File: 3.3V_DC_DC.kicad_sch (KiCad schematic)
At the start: 10 parts, among them U5 MT2492

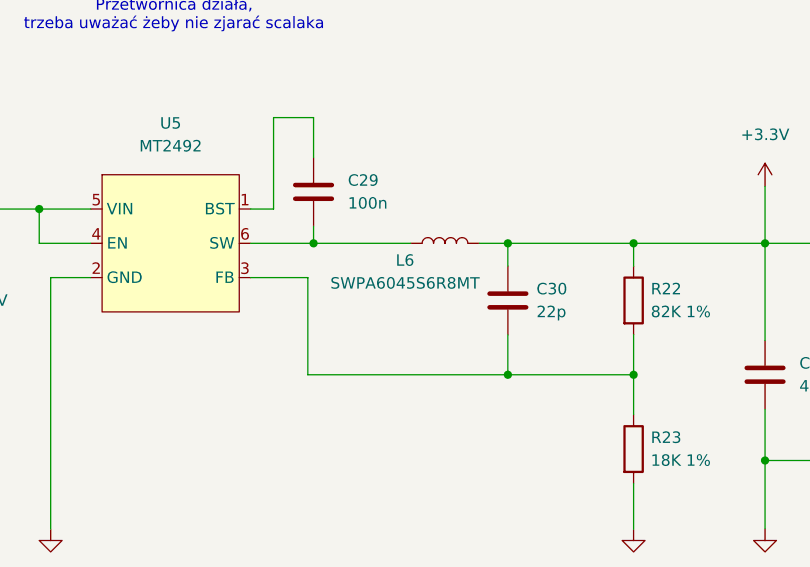
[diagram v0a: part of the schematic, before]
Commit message: Update schematic for V1.1
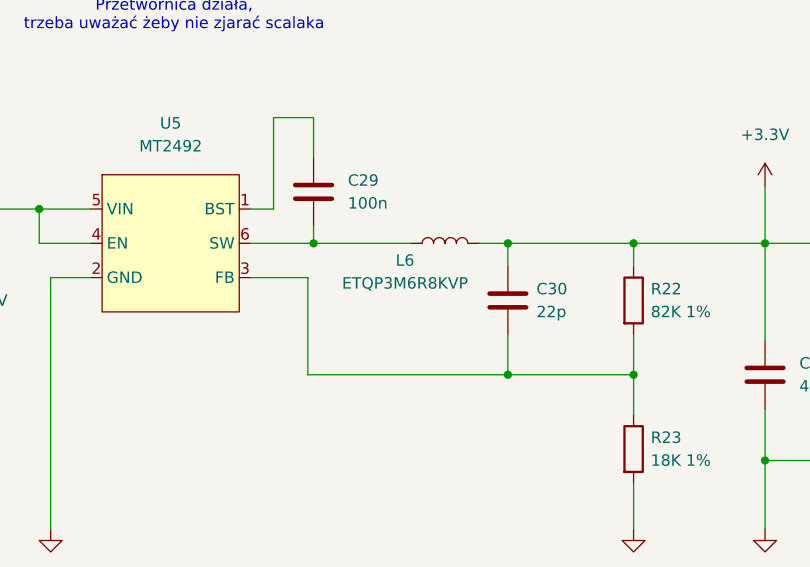
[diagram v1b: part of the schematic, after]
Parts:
- L6: value SWPA6045S6R8MT -> ETQP3M6R8KVP; footprint SWPA6045S6R8MT:SWPA6045S6R8MT -> panasonic_coil:IND_PCC-M0530M-LP_PAN; LCSC C57254 -> C412311
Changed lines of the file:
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@@
 			)
 		)
-		(property "Value" "SWPA6045S6R8MT"
+		(property "Value" "ETQP3M6R8KVP"
 			(at 132.08 58.42 90)
 			(effects
@@
 			)
 		)
-		(property "Footprint" "SWPA6045S6R8MT:SWPA6045S6R8MT"
+		(property "Footprint" "panasonic_coil:IND_PCC-M0530M-LP_PAN"
 			(at 136.525 53.975 0)
 			(effects
@@
 			)
 		)
-		(property "Datasheet" ""
+		(property "Datasheet" "https://www.lcsc.com/datasheet/lcsc_datasheet_1912111437_PANASONIC-ETQP3M6R8KVP_C412311.pdf"
 			(at 136.525 53.975 0)
 			(effects
@@
 			)
 		)
-		(property "LCSC" "C57254"
+		(property "LCSC" "C412311"
 			(at 136.525 53.975 90)
 			(effects

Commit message: DO the bulk of rev 1.2 layout
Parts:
- D7: value 3.3 -> PESD3V3L1BA; footprint Diode_SMD:D_SMA-SMB_Universal_Handsoldering -> Diode_SMD:D_SOD-323
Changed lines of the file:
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@@
 			)
 		)
-		(property "Value" "3.3"
+		(property "Value" "PESD3V3L1BA"
 			(at 193.675 67.9449 90)
 			(effects
@@
 			)
 		)
-		(property "Footprint" "Diode_SMD:D_SMA-SMB_Universal_Handsoldering"
+		(property "Footprint" "Diode_SMD:D_SOD-323"
 			(at 191.135 66.675 0)
 			(effects

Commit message: Use kicad symbol for the optotransistor
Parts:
- L6: footprint panasonic_coil:IND_PCC-M0530M-LP_PAN -> project_footprints:IND_PCC-M0530M-LP_PAN
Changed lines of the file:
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@@
 			)
 		)
-		(property "Footprint" "panasonic_coil:IND_PCC-M0530M-LP_PAN"
+		(property "Footprint" "project_footprints:IND_PCC-M0530M-LP_PAN"
 			(at 136.525 53.975 0)
 			(effects

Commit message: BOM updates
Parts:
- D7: LCSC (none) -> C2687129

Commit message: Zamkonator rev 1.3
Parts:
- renumbered C27 to C29, C28 to C30, C29 to C31, C30 to C32, C31 to C33, D7 to D12, R22 to R29, R23 to R30, U5 to U6
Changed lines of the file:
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@@
 		(dnp no)
 		(fields_autoplaced yes)
-		(property "Reference" "#PWR042"
+		(property "Reference" "#PWR080"
 			(at 172.085 92.075 0)
 			(hide yes)
@@
 			(project "Zamkonator"
 				(path "/727d6c0a-a0ef-4feb-9656-3db3cb90564a/8f37bbe0-86b5-4d99-ba58-4681edf3128e"
-					(reference "#PWR042")
+					(reference "#PWR080")
 					(unit 1)
 				)
@@
 		(dnp no)
 		(fields_autoplaced yes)
-		(property "Reference" "#PWR041"
+		(property "Reference" "#PWR079"
 			(at 172.085 51.435 0)
 			(hide yes)
@@
 			(project "Zamkonator"
 				(path "/727d6c0a-a0ef-4feb-9656-3db3cb90564a/8f37bbe0-86b5-4d99-ba58-4681edf3128e"
-					(reference "#PWR041")
+					(reference "#PWR079")
 					(unit 1)
 				)
@@
 		(dnp no)
 		(fields_autoplaced yes)
-		(property "Reference" "#PWR037"
+		(property "Reference" "#PWR075"
 			(at 59.055 92.075 0)
 			(hide yes)
@@
 			(project "Zamkonator"
 				(path "/727d6c0a-a0ef-4feb-9656-3db3cb90564a/8f37bbe0-86b5-4d99-ba58-4681edf3128e"
-					(reference "#PWR037")
+					(reference "#PWR075")
 					(unit 1)
 				)
@@
 		(dnp no)
 		(fields_autoplaced yes)
-		(property "Reference" "D7"
+		(property "Reference" "D12"
 			(at 193.675 65.4049 90)
 			(show_name no)
@@
 			(project "Zamkonator"
 				(path "/727d6c0a-a0ef-4feb-9656-3db3cb90564a/8f37bbe0-86b5-4d99-ba58-4681edf3128e"
-					(reference "D7")
+					(reference "D12")
 					(unit 1)
 				)
@@
 		(dnp no)
 		(fields_autoplaced yes)
-		(property "Reference" "C31"
+		(property "Reference" "C33"
 			(at 175.895 67.3099 0)
 			(show_name no)
@@
 			(project "Zamkonator"
 				(path "/727d6c0a-a0ef-4feb-9656-3db3cb90564a/8f37bbe0-86b5-4d99-ba58-4681edf3128e"
-					(reference "C31")
+					(reference "C33")
 					(unit 1)
 				)
@@
 		(dnp no)
 		(fields_autoplaced yes)
-		(property "Reference" "U5"
+		(property "Reference" "U6"
 			(at 106.045 40.64 0)
 			(show_name no)
@@
 			(project "Zamkonator"
 				(path "/727d6c0a-a0ef-4feb-9656-3db3cb90564a/8f37bbe0-86b5-4d99-ba58-4681edf3128e"
-					(reference "U5")
+					(reference "U6")
 					(unit 1)
 				)
@@
 		(dnp no)
 		(fields_autoplaced yes)
-		(property "Reference" "C29"
+		(property "Reference" "C31"
 			(at 125.73 46.9899 0)
 			(show_name no)
@@
 			(project "Zamkonator"
 				(path "/727d6c0a-a0ef-4feb-9656-3db3cb90564a/8f37bbe0-86b5-4d99-ba58-4681edf3128e"
-					(reference "C29")
+					(reference "C31")
 					(unit 1)
 				)
@@
 		(dnp no)
 		(fields_autoplaced yes)
-		(property "Reference" "R22"
+		(property "Reference" "R29"
 			(at 159.385 59.0549 0)
 			(show_name no)
@@
 			(project "Zamkonator"
 				(path "/727d6c0a-a0ef-4feb-9656-3db3cb90564a/8f37bbe0-86b5-4d99-ba58-4681edf3128e"
-					(reference "R22")
+					(reference "R29")
 					(unit 1)
 				)
@@
 		(dnp no)
 		(fields_autoplaced yes)
-		(property "Reference" "#PWR039"
+		(property "Reference" "#PWR077"
 			(at 92.71 92.075 0)
 			(hide yes)
@@
 			(project "Zamkonator"
 				(path "/727d6c0a-a0ef-4feb-9656-3db3cb90564a/8f37bbe0-86b5-4d99-ba58-4681edf3128e"
-					(reference "#PWR039")
+					(reference "#PWR077")
 					(unit 1)
 				)
@@
 		(dnp no)
 		(fields_autoplaced yes)
-		(property "Reference" "#PWR038"
+		(property "Reference" "#PWR076"
 			(at 76.835 92.075 0)
 			(hide yes)
@@
 			(project "Zamkonator"
 				(path "/727d6c0a-a0ef-4feb-9656-3db3cb90564a/8f37bbe0-86b5-4d99-ba58-4681edf3128e"
-					(reference "#PWR038")
+					(reference "#PWR076")
 					(unit 1)
 				)
@@
 		(dnp no)
 		(fields_autoplaced yes)
-		(property "Reference" "#PWR040"
+		(property "Reference" "#PWR078"
 			(at 157.48 92.075 0)
 			(hide yes)
@@
 			(project "Zamkonator"
 				(path "/727d6c0a-a0ef-4feb-9656-3db3cb90564a/8f37bbe0-86b5-4d99-ba58-4681edf3128e"
-					(reference "#PWR040")
+					(reference "#PWR078")
 					(unit 1)
 				)
@@
 		(dnp no)
 		(fields_autoplaced yes)
-		(property "Reference" "C27"
+		(property "Reference" "C29"
 			(at 62.865 57.5309 0)
 			(show_name no)
@@
 			(project "Zamkonator"
 				(path "/727d6c0a-a0ef-4feb-9656-3db3cb90564a/8f37bbe0-86b5-4d99-ba58-4681edf3128e"
-					(reference "C27")
+					(reference "C29")
 					(unit 1)
 				)
@@
 		(dnp no)
 		(fields_autoplaced yes)
-		(property "Reference" "C28"
+		(property "Reference" "C30"
 			(at 80.645 57.7849 0)
 			(show_name no)
@@
 			(project "Zamkonator"
 				(path "/727d6c0a-a0ef-4feb-9656-3db3cb90564a/8f37bbe0-86b5-4d99-ba58-4681edf3128e"
-					(reference "C28")
+					(reference "C30")
 					(unit 1)
 				)
@@
 		(dnp no)
 		(fields_autoplaced yes)
-		(property "Reference" "R23"
+		(property "Reference" "R30"
 			(at 159.385 75.5649 0)
 			(show_name no)
@@
 			(project "Zamkonator"
 				(path "/727d6c0a-a0ef-4feb-9656-3db3cb90564a/8f37bbe0-86b5-4d99-ba58-4681edf3128e"
-					(reference "R23")
+					(reference "R30")
 					(unit 1)
 				)
@@
 		(dnp no)
 		(fields_autoplaced yes)
-		(property "Reference" "C30"
+		(property "Reference" "C32"
 			(at 146.685 59.0549 0)
 			(show_name no)
@@
 			(project "Zamkonator"
 				(path "/727d6c0a-a0ef-4feb-9656-3db3cb90564a/8f37bbe0-86b5-4d99-ba58-4681edf3128e"
-					(reference "C30")
+					(reference "C32")
 					(unit 1)
 				)

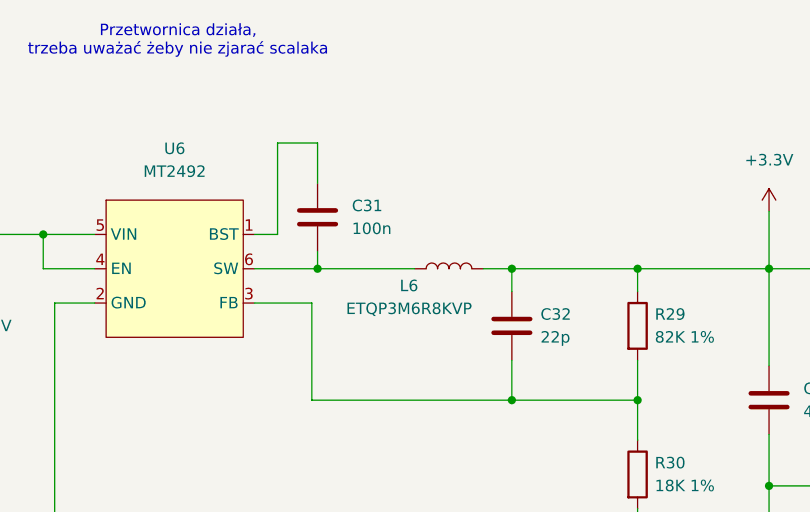
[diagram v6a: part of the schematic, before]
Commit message: Rev 1.3, BOM optimizations
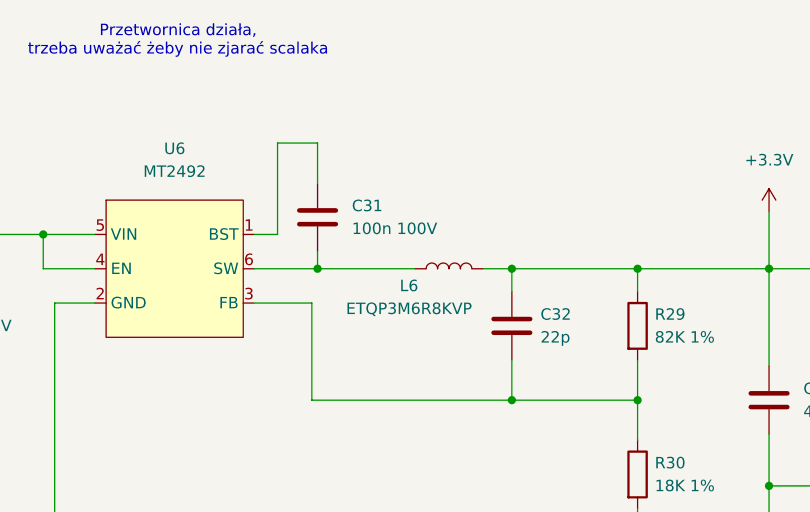
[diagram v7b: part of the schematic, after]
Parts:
- C31: value 100n -> 100n 100V
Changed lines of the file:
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@@
 			)
 		)
-		(property "Value" "100n"
+		(property "Value" "100n 100V"
 			(at 125.73 49.5299 0)
 			(show_name no)
